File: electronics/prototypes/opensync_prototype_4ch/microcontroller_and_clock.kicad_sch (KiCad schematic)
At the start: 43 parts, among them J12 SM03B-SRSS-TB, J13 61611042121502, SW1 SW_Push, SW2 SW_Push, U2 RP2354_80QFN, Y1 ABM8-272-T3

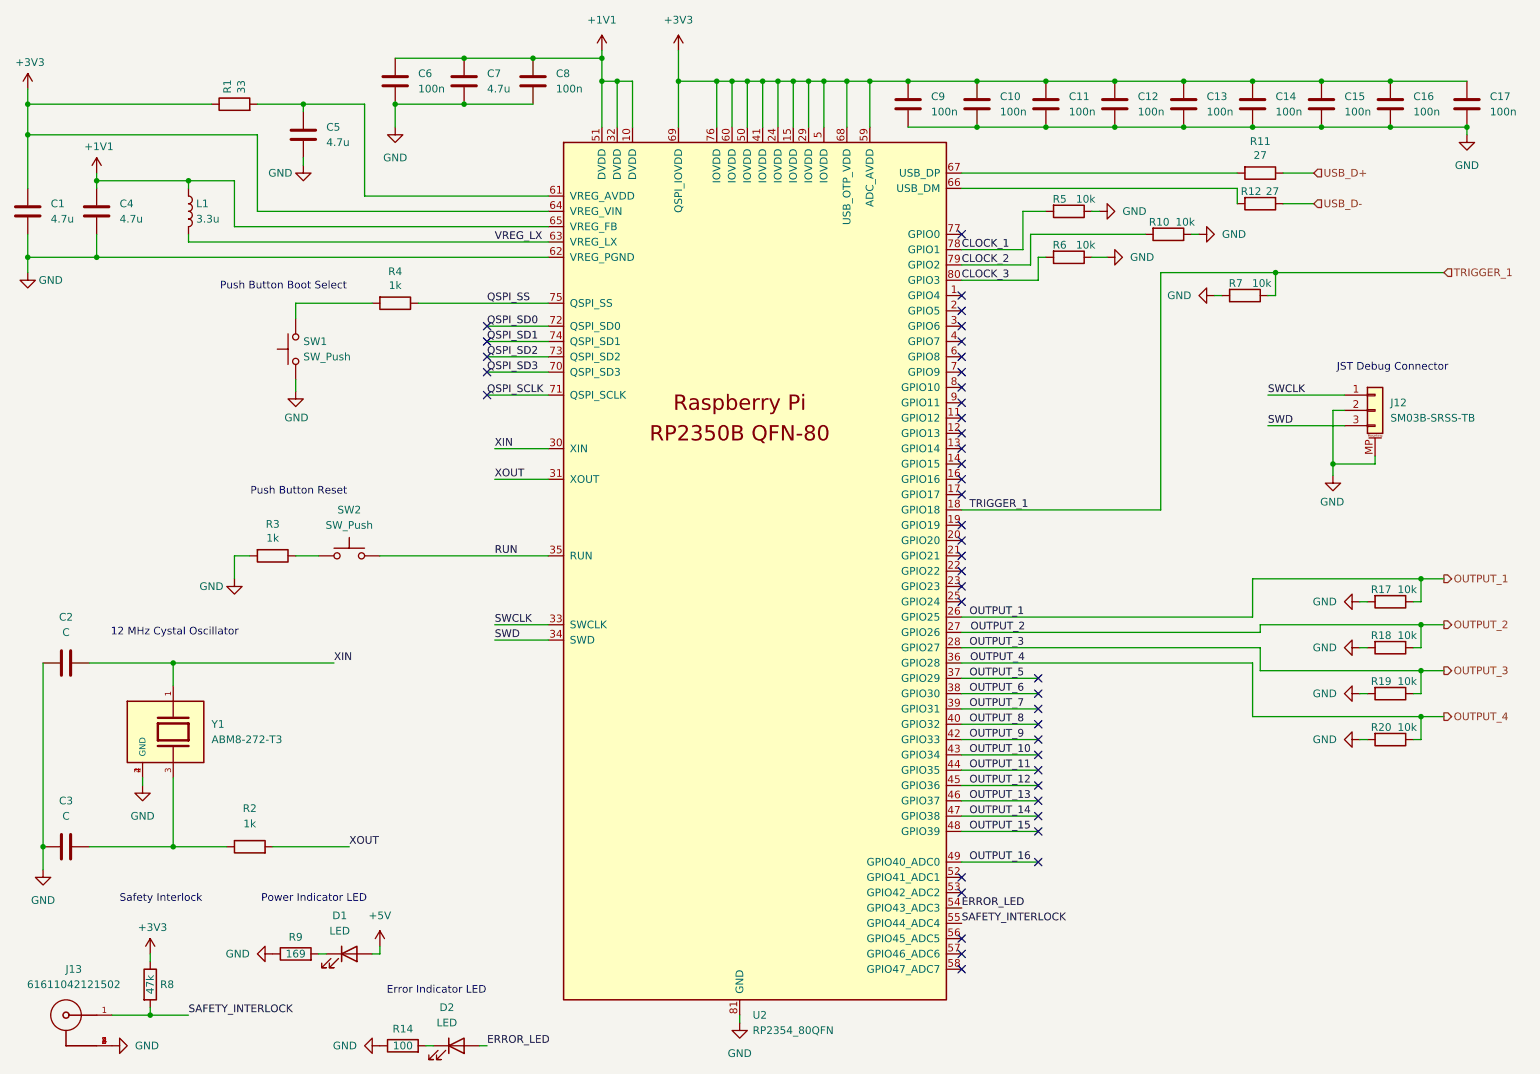
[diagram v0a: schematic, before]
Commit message: Added part numbers
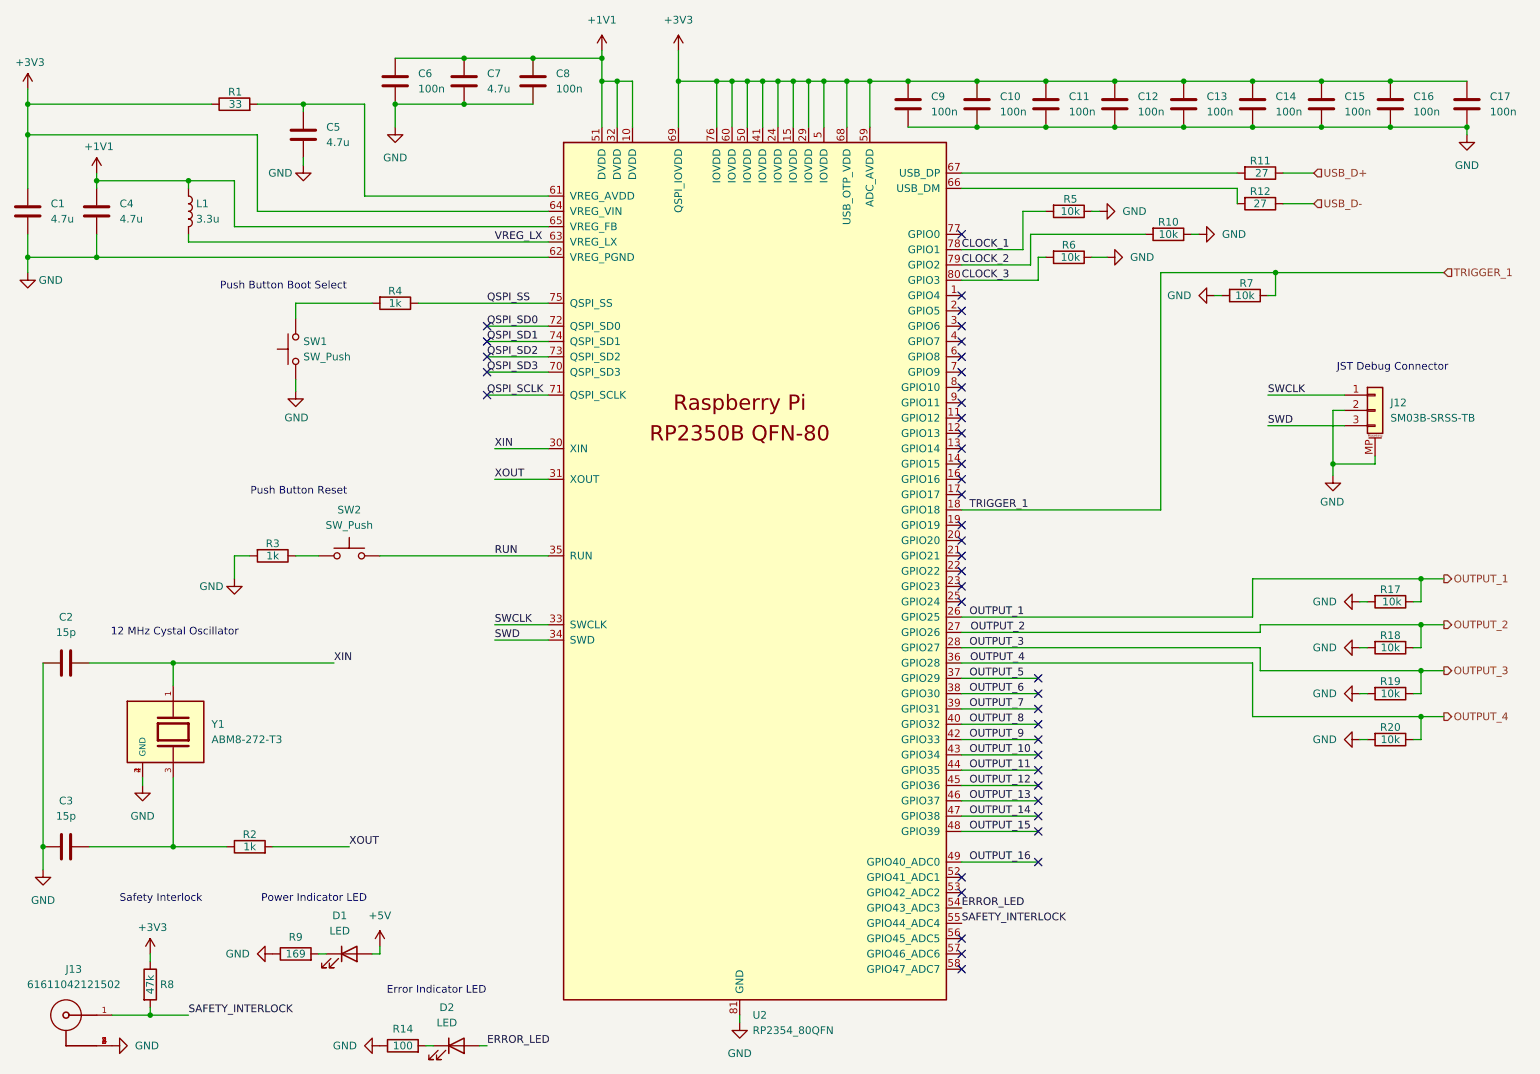
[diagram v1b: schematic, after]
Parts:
- C1, C4, C5: LCSC (none) -> C326586
- C10, C11, C12, C13, C14, C15, C16, C17, C6, C7, C8, C9: LCSC (none) -> C60474
- C2, C3: value C -> 15p; LCSC (none) -> C326803
- L1: LCSC (none) -> C42411119
- R1: LCSC (none) -> C844506
- R10, R17, R18, R19, R20, R5, R6, R7: LCSC (none) -> C71617
- R11, R12: LCSC (none) -> C4162575
- R2, R3, R4: LCSC (none) -> C313354
- R8: LCSC (none) -> C176117
- U2: LCSC (none) -> C39843328
- Y1: LCSC (none) -> C20625731

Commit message: More prototyping
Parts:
- removed D1, D2: LED, LED_SMD:LED_0603_1608Metric, symbol Device:LED
- removed J13: 61611042121502, 61611042121502:61611042121502, symbol 61611042121502:61611042121502
- removed R14: 100, Resistor_SMD:R_0402_1005Metric, symbol Device:R
- removed R8: 47k, Resistor_SMD:R_0402_1005Metric, symbol Device:R
- removed R9: 169, Resistor_SMD:R_0402_1005Metric, symbol Device:R
- J12: LCSC (none) -> C160403
- SW1, SW2: LCSC (none) -> C5504987
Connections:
- net SAFETY_INTERLOCK: now also U2.56 (GPIO45_ADC5); no longer U2.55 (GPIO44_ADC4)
- new net INTERLOCK_LED: U2.55 (GPIO44_ADC4)
- no-connect marks 43 -> 42
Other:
- note removed: "Error Indicator LED"
- note removed: "Power Indicator LED"
- note removed: "Safety Interlock"
- moved on the sheet: R10
